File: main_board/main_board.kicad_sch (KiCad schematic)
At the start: 13 parts, among them J1 CON-SMA-EDGE-S, U2 TS5A4624DCKR, U4 TS5A4624DCKR

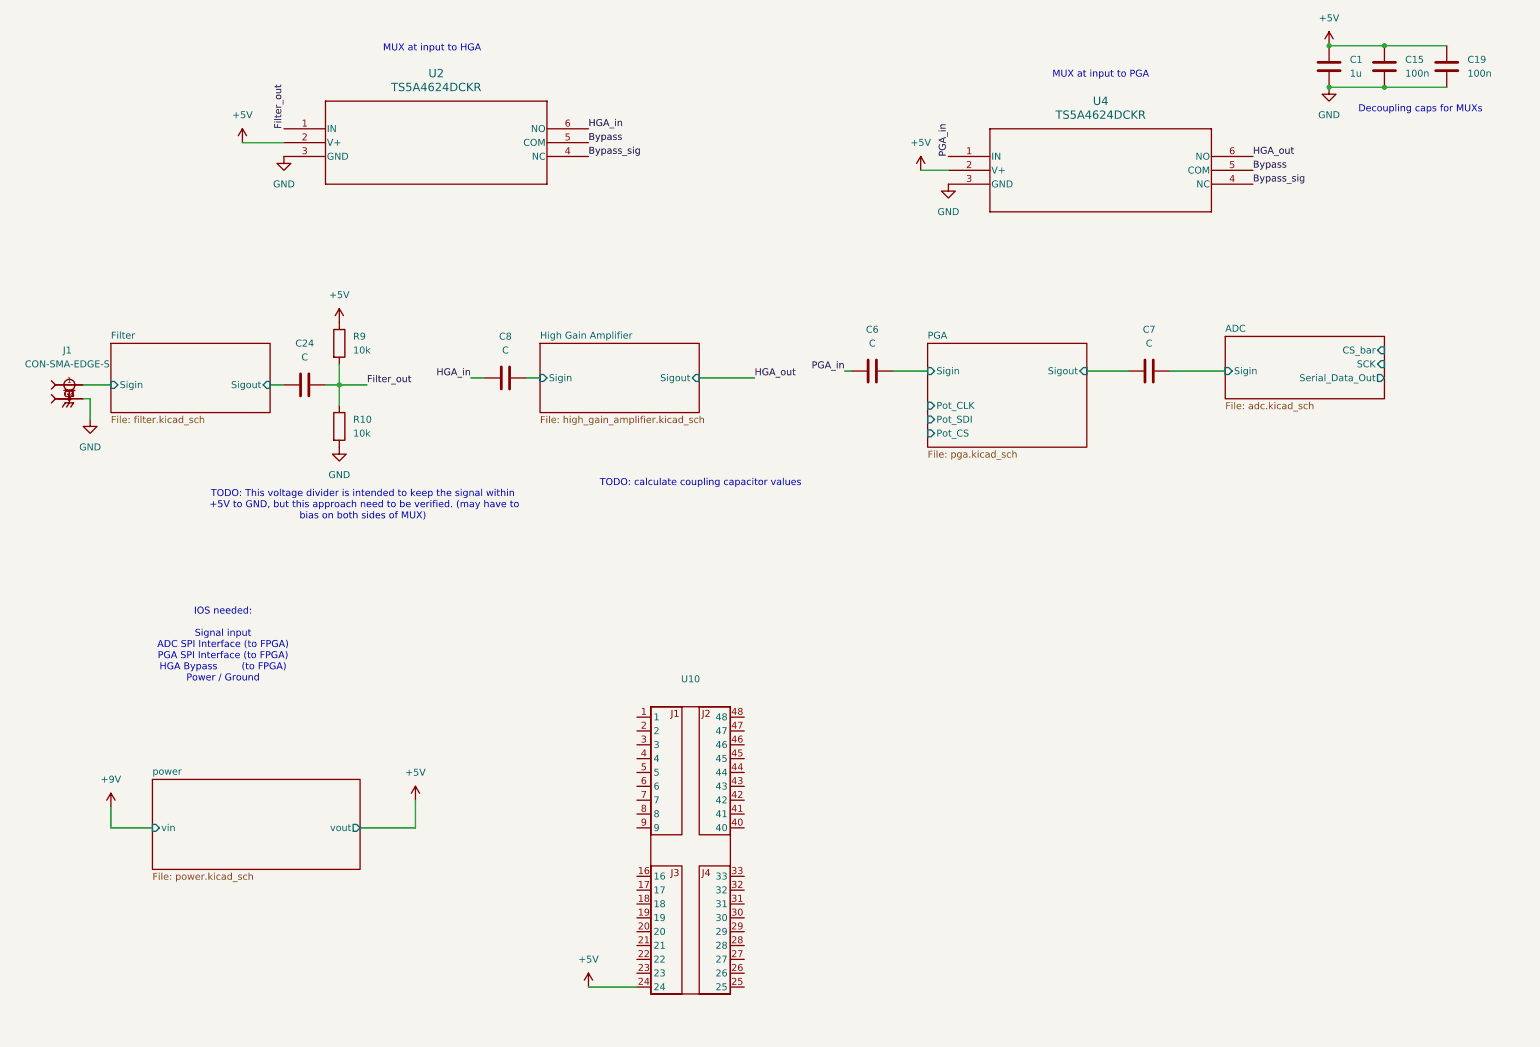
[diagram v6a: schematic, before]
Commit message: Added PCBway drc ruleset, connected mux IO, ADC SPI interface, Pot SPI interface & 0603 footprints to all passive devices.
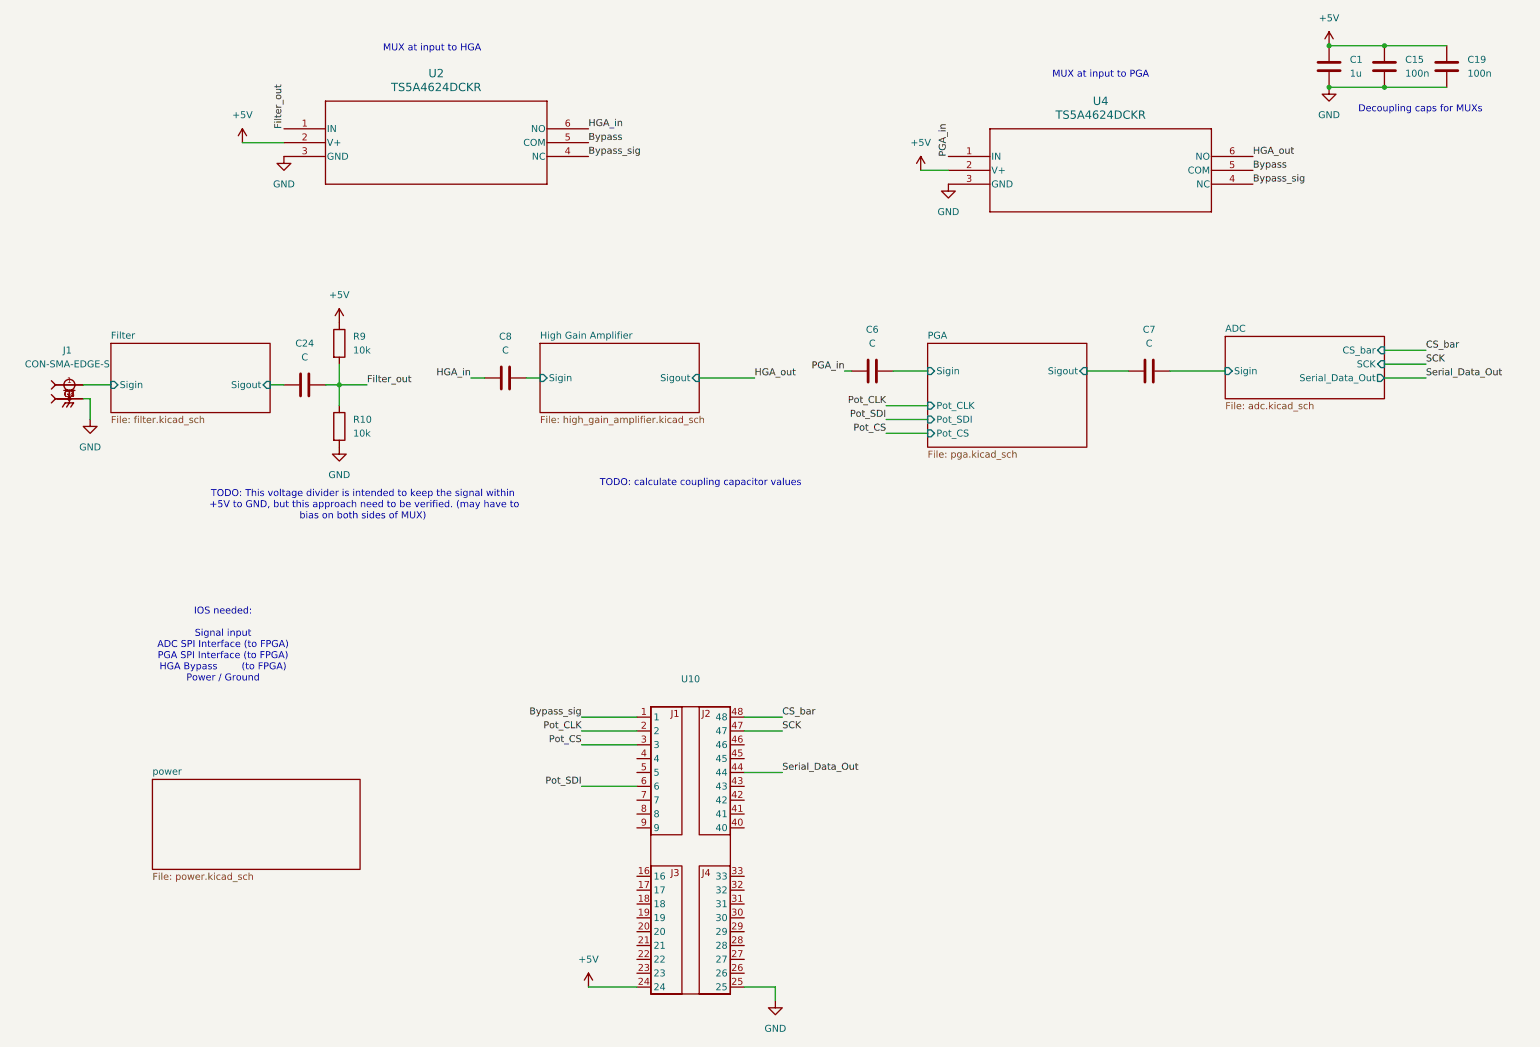
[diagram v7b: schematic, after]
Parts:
- C1, C15, C19, C24, C6, C7, C8: footprint (none) -> Capacitor_SMD:C_0603_1608Metric
- J1: footprint CON-SMA-EDGE-S:RFSOLUTIONS_CON-SMA-EDGE-S -> SMA_male_fp:RFSOLUTIONS_CON-SMA-EDGE-S
- R10, R9: footprint (none) -> Resistor_SMD:R_0603_1608Metric
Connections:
- net Bypass_sig: now also U10.1
- net GND: now also U10.25
- net Pot_CLK: now reaches U10.2
- net Pot_CS: now reaches U10.3
- net Serial_Data_Out: now reaches U10.44
- net SCK: now reaches U10.47
- net CS_bar: now reaches U10.48
- net Pot_SDI: now reaches U10.6
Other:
- sheet power ports: added none; removed vin, vout

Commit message: Finalized last schematic changes, awaing group approval.
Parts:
- C24: value C -> 22n
- C6: value C -> .15u
- C7, C8: value C -> 68p
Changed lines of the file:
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@@
 			)
 		)
-		(property "Value" "C"
+		(property "Value" ".15u"
 			(at 163.83 73.66 90)
 			(effects
@@
 			)
 		)
-		(property "Value" "C"
+		(property "Value" "68p"
 			(at 96.52 74.93 90)
 			(effects
@@
 			)
 		)
-		(property "Value" "C"
+		(property "Value" "22n"
 			(at 59.69 76.2 90)
 			(effects
@@
 			)
 		)
-		(property "Value" "C"
+		(property "Value" "68p"
 			(at 214.63 73.66 90)
 			(effects
